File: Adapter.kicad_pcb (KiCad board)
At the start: 2 copper layers, 33 x 19.5 mm, 7 parts, among them J1 USB_B_Micro, J2 2040210-1, J3 USB_C_Receptacle, J4 Conn_01x04

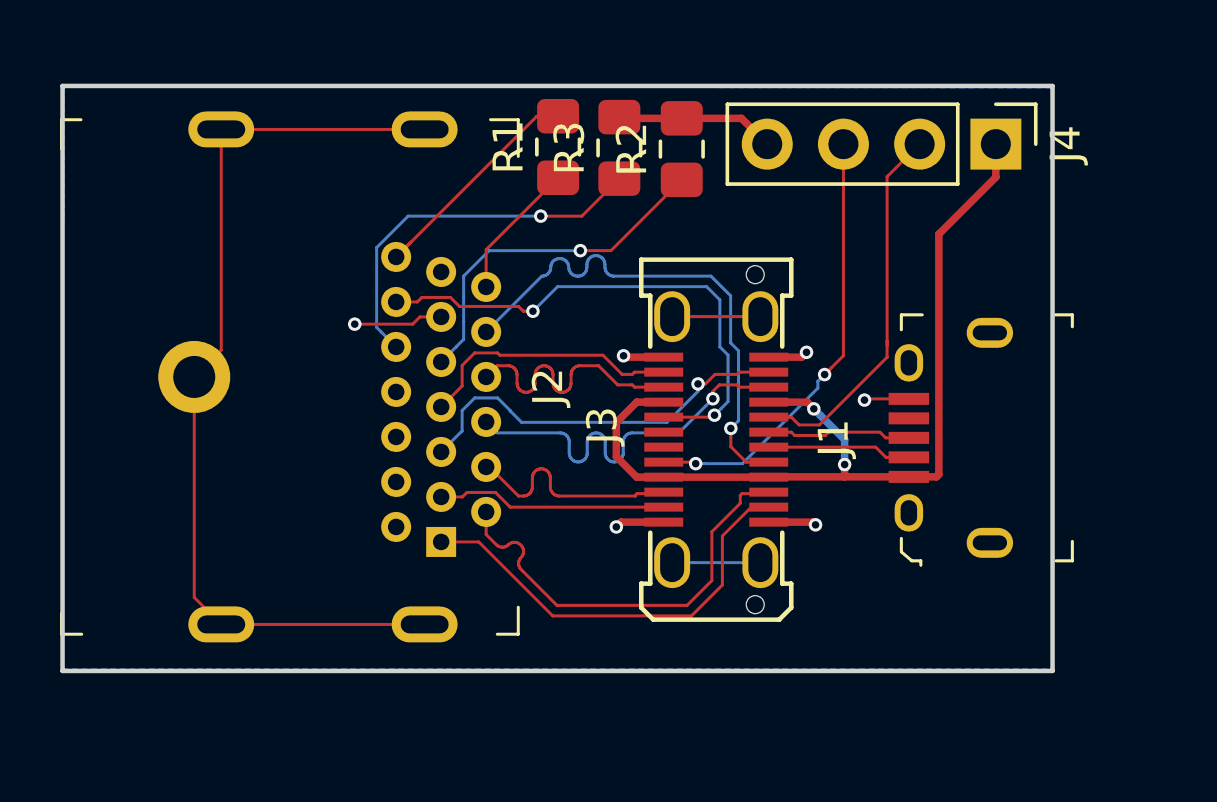
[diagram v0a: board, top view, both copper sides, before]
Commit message: New design with DP and USB-mB on same side
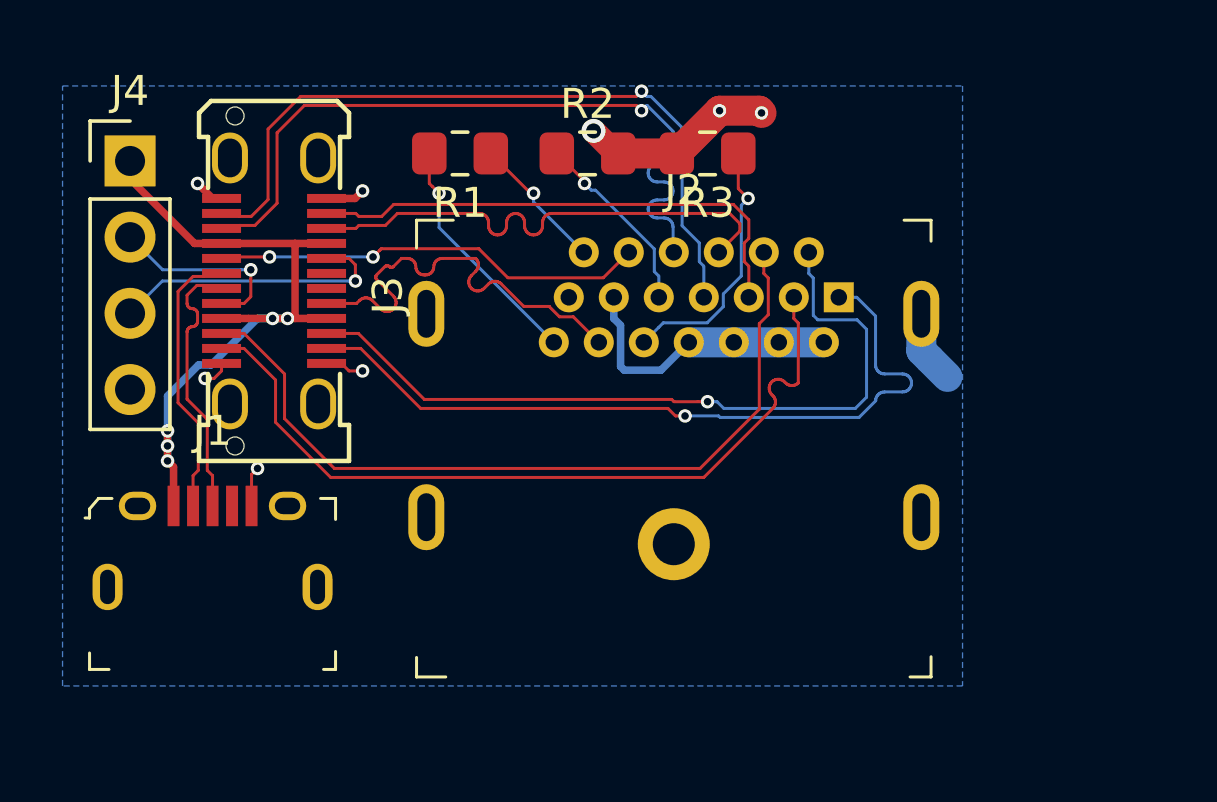
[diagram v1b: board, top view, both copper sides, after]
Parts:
- moved J4 28.9 mm to (14.8, 15.0), turned to 0 degrees
- moved J1 23.3 mm to (17.5, 26.5), turned to 0 degrees
- moved J3 18.1 mm to (18.2, 19.0), turned to 90 degrees
- moved J2 16.9 mm to (32.9, 27.8), turned to 0 degrees
- moved R1 3.28 mm to (25.8, 14.8), turned to 180 degrees
- moved R2 3.14 mm to (30.0, 14.8), turned to 0 degrees
- moved R3 2.95 mm to (34.0, 14.8), turned to 180 degrees
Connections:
- J2 pad 1: /DP0+ -> /DP3+
- J2 pad 10: /DP3+ -> /DP0+
- J2 pad 12: /DP3- -> /DP0-
- J2 pad 3: /DP0- -> /DP3-
- J2 pad 4: /DP1+ -> /DP2+
- J2 pad 6: /DP1- -> /DP2-
- J2 pad 7: /DP2+ -> /DP1+
- J2 pad 9: /DP2- -> /DP1-
- J2 pad SH: Net-(J2-PadSH) -> GND
- J3 pad S1: Net-(J3-PadS1) -> GND
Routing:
- net Net-(J2-PadSH): track 30.8 -> 0.00 mm
- net /DP3+: track 8.89 -> 25.7 mm, vias 0 -> 1
- net /DP3-: track 8.89 -> 25.6 mm, vias 0 -> 1
- net /DP2+: track 13.3 -> 26.8 mm, vias 1 -> 0
- net /DP2-: track 13.3 -> 26.9 mm, vias 1 -> 0
- net /DP0+: track 14.4 -> 25.0 mm, vias 0 -> 1
- net /DP0-: track 14.5 -> 25.0 mm, vias 0 -> 1
- net VBUS: track 34.8 -> 24.9 mm, vias 2 -> 5
- net /DP1-: track 7.69 -> 17.2 mm
- net /DP1+: track 7.69 -> 17.2 mm
- net GND: track 15.7 -> 24.5 mm, vias 6 -> 8
- net /CC1: track 12.7 -> 6.44 mm, vias 0 -> 1
- net Net-(J3-PadS1): track 5.88 -> 0.00 mm
- net /CONFIG1: track 11.8 -> 6.29 mm
- net /CC2: track 14.7 -> 9.55 mm, vias 2 -> 1
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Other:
- board outline removed
- rule pad_to_mask_clearance: 0.2 -> 0
- rule via_min_drill: 0.2 -> 0.25

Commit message: 4-Layer-Design with correct DP Lane polarity and impedance matching
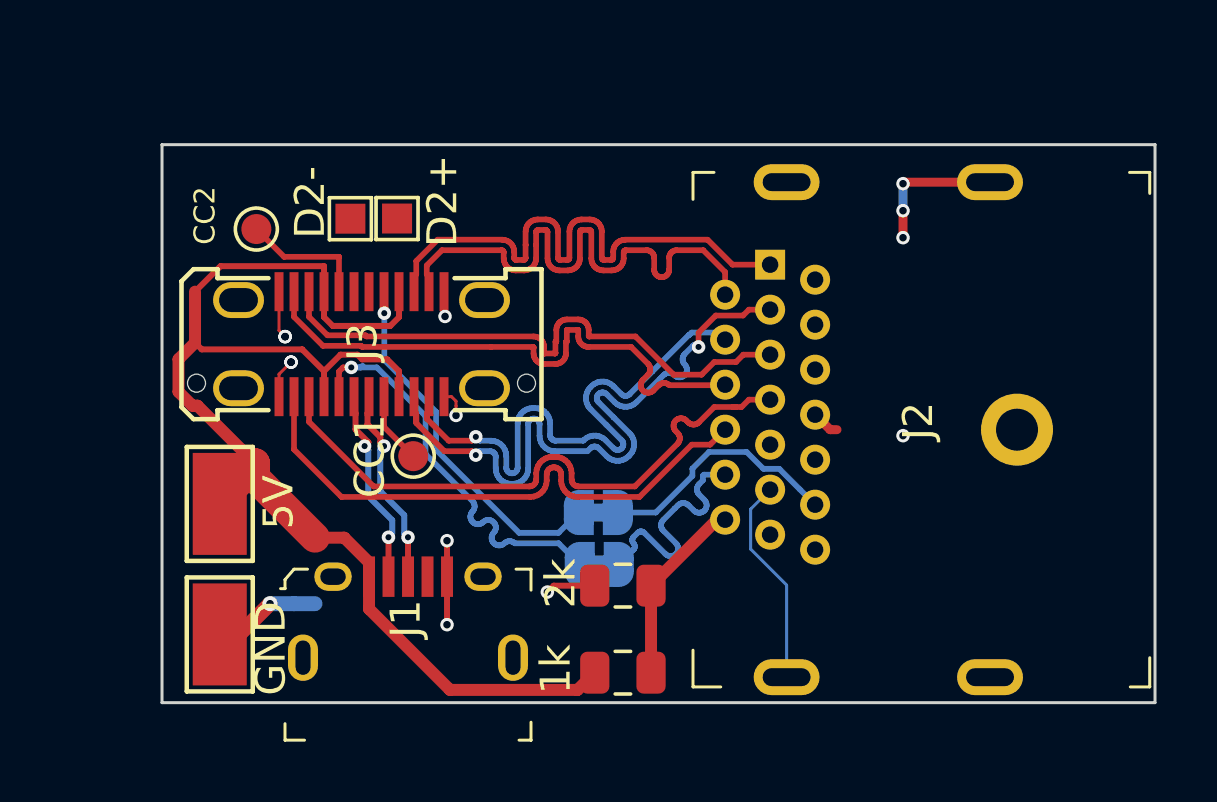
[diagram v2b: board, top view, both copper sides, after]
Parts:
- removed J4: Conn_01x04, Connector_PinHeader_2.54mm:PinHeader_1x04_P2.54mm_Vertical
- removed R1, R2, R3: R, Resistor_SMD:R_0805_2012Metric_Pad1.15x1.40mm_HandSolder
- added 1k: 1k, Resistor_SMD:R_0805_2012Metric, F.Cu at (31.2, 32.1)
- added 2k: 2k, Resistor_SMD:R_0805_2012Metric, F.Cu at (31.2, 29.2)
- added 5V: Conn_01x01, TestPoint:TestPoint_Keystone_5015_Micro-Minature, F.Cu at (17.7, 26.4)
- added CC1: Conn_01x01, TestPoint:TestPoint_Pad_D1.0mm, F.Cu at (24.2, 24.8)
- added CC2: Conn_01x01, TestPoint:TestPoint_Pad_D1.0mm, F.Cu at (19.0, 17.3)
- added D2+: Conn_01x01, TestPoint:TestPoint_Pad_1.0x1.0mm, F.Cu at (23.6, 16.9)
- added D2-: Conn_01x01, TestPoint:TestPoint_Pad_1.0x1.0mm, F.Cu at (22.1, 16.9)
- added GND: Conn_01x01, TestPoint:TestPoint_Keystone_5015_Micro-Minature, F.Cu at (17.7, 30.8)
- added JP1: Jumper, Jumper:SolderJumper-2_P1.3mm_Bridged_RoundedPad1.0x1.5mm, B.Cu at (30.4, 28.4)
- added JP2: Jumper, Jumper:SolderJumper-2_P1.3mm_Bridged_RoundedPad1.0x1.5mm, B.Cu at (30.4, 26.7)
- moved J2 12.1 mm to (44.3, 24.0), turned to 90 degrees
- moved J1 6.93 mm to (24.0, 28.9)
- moved J3 5.42 mm to (22.5, 22.4), turned to 180 degrees
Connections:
- J2 pad 1: /DP3+ -> /DP3-
- J2 pad 10: /DP0+ -> /DP0-
- J2 pad 12: /DP0- -> /DP0+
- J2 pad 3: /DP3- -> /DP3+
- J2 pad 4: /DP2+ -> /DP2-
- J2 pad 6: /DP2- -> /DP2+
- J2 pad 7: /DP1+ -> /DP1-
- J2 pad 9: /DP1- -> /DP1+
- J3 pad A8: /AUX+ -> /pAUX+
- J3 pad B6: Net-(J3-PadB6) -> /D2+
- J3 pad B7: Net-(J3-PadB7) -> /D2-
- J3 pad B8: /AUX- -> /pAUX-
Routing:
- net VBUS: track 24.9 -> 44.1 mm, vias 5 -> 0
- net /pAUX+: track 0.00 -> 13.9 mm, vias 0 -> 1
- net /pAUX-: track 0.00 -> 12.2 mm, vias 0 -> 1
- net /CONFIG2: track 8.73 -> 0.00 mm, vias 1 -> 0
- net /DP_PWR: track 8.01 -> 0.00 mm, vias 1 -> 0
- net /DP2+: track 26.8 -> 19.7 mm, vias 0 -> 1
- net /DP3+: track 25.7 -> 19.0 mm, vias 1 -> 0
- net /DP3-: track 25.6 -> 19.0 mm, vias 1 -> 0
- net /CONFIG1: track 6.29 -> 0.00 mm, vias 1 -> 0
- net /AUX+: track 14.5 -> 8.22 mm, vias 2 -> 0
- net /AUX-: track 14.5 -> 8.28 mm
- net /DP0+: track 25.0 -> 19.1 mm, vias 1 -> 0
- net /CC2: track 9.55 -> 4.30 mm, vias 1 -> 0
- net /DP0-: track 25.0 -> 20.4 mm, vias 1 -> 0
- net /CC1: track 6.44 -> 2.39 mm, vias 1 -> 0
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- added copper zone on In1.Cu, net GND
- added copper zone on In2.Cu, net GND
- removed copper zone on B.Cu, net GND
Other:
- board outline added: 33.1 x 18.6 mm
- copper layers 2 -> 4
- net class Default: trace_width 0.1 -> 0.19; via_drill 0.25 -> 0.2
- net class Power added: clearance 0.1, trace_width 0.5, via_dia 0.7, via_drill 0.4
- rule via_min_drill: 0.25 -> 0.2

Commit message: cosmetic changes
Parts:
- removed JP1, JP2: Jumper, Jumper:SolderJumper-2_P1.3mm_Bridged_RoundedPad1.0x1.5mm
- added AUX+: Jumper, Jumper:SolderJumper-2_P1.3mm_Bridged_RoundedPad1.0x1.5mm, B.Cu at (30.4, 28.4)
- added AUX-: Jumper, Jumper:SolderJumper-2_P1.3mm_Bridged_RoundedPad1.0x1.5mm, B.Cu at (30.4, 26.7)
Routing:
- net VBUS: track 44.1 -> 48.3 mm
- net /D2-: track 0.00 -> 2.82 mm
- net /D2+: track 0.00 -> 2.48 mm
- net /pAUX-: track 12.2 -> 13.1 mm
- net /pAUX+: track 13.9 -> 13.2 mm
- net /DP0-: track 20.4 -> 21.1 mm
- net GND: track 25.4 -> 25.5 mm, vias 13 -> 11

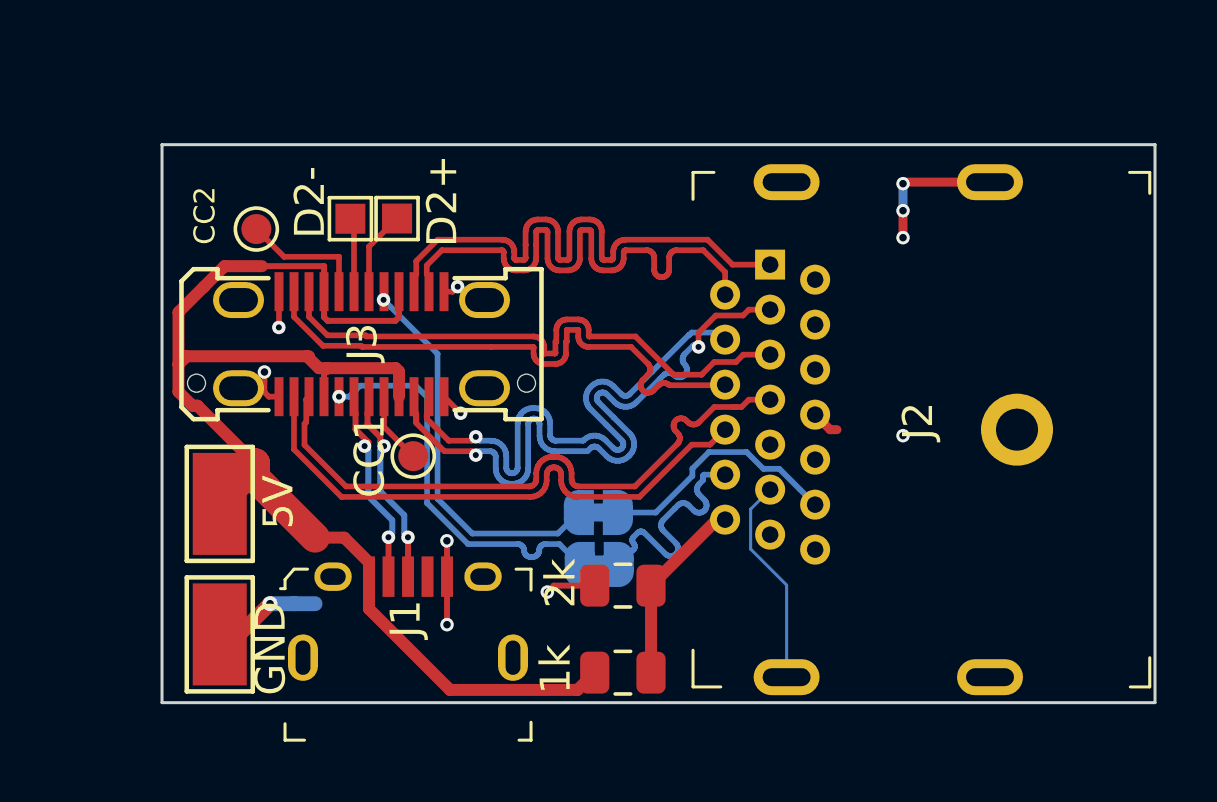
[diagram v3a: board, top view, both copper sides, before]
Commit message: Re-matched and DRCed for OSHPark's 4 Layer Process
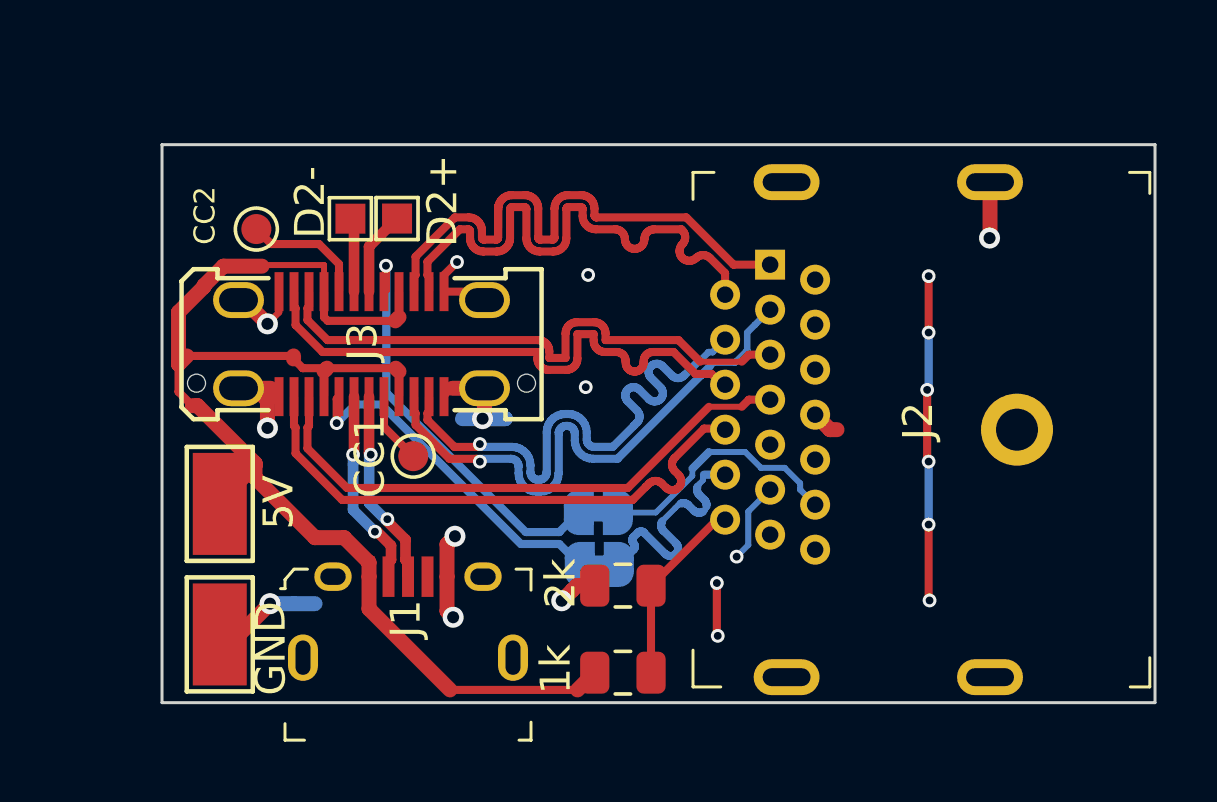
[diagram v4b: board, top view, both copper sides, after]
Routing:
- net GND: track 25.5 -> 39.7 mm, vias 11 -> 20
- net /DP2-: track 23.2 -> 19.1 mm, vias 2 -> 1
- net VBUS: track 48.3 -> 44.2 mm
- net /DP0-: track 21.1 -> 18.9 mm
- net /pAUX+: track 13.2 -> 11.5 mm
- net /DP3-: track 19.0 -> 20.0 mm
- net /DP2+: track 19.7 -> 19.0 mm
- net /pAUX-: track 13.1 -> 13.7 mm
- net (no net): vias 1 -> 0
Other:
- net class Default: clearance 0.1 -> 0.127; trace_width 0.19 -> 0.27; via_dia 0.45 -> 0.46; via_drill 0.2 -> 0.26
- net class Power: clearance 0.1 -> 0.127
- net class USB added: clearance 0.127, trace_width 0.357, via_dia 0.46, via_drill 0.26
- rule trace_clearance: 0.1 -> 0.127
- rule via_min_drill: 0.2 -> 0.26
- rule via_min_size: 0.45 -> 0.36
